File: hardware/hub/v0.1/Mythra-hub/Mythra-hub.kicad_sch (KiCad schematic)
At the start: 2 parts, among them J2 Molex Power Input, U1 TUSB8042A

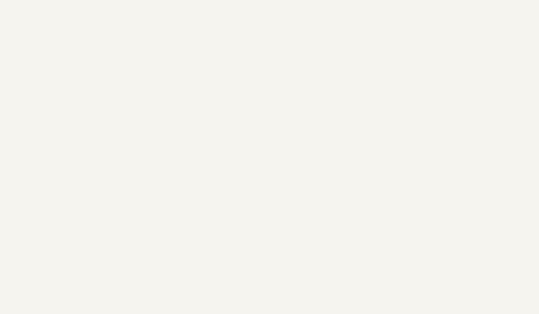
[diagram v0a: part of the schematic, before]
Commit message: Added power delivery control to the DFPs
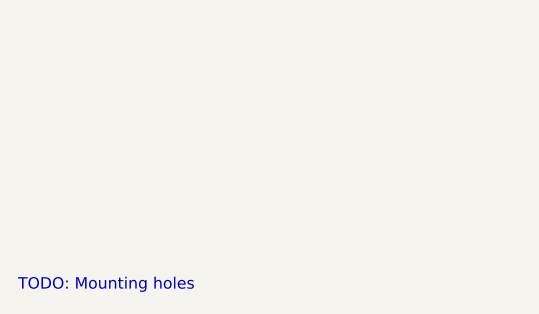
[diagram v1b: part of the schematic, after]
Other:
- note added: "TODO: Mounting holes"

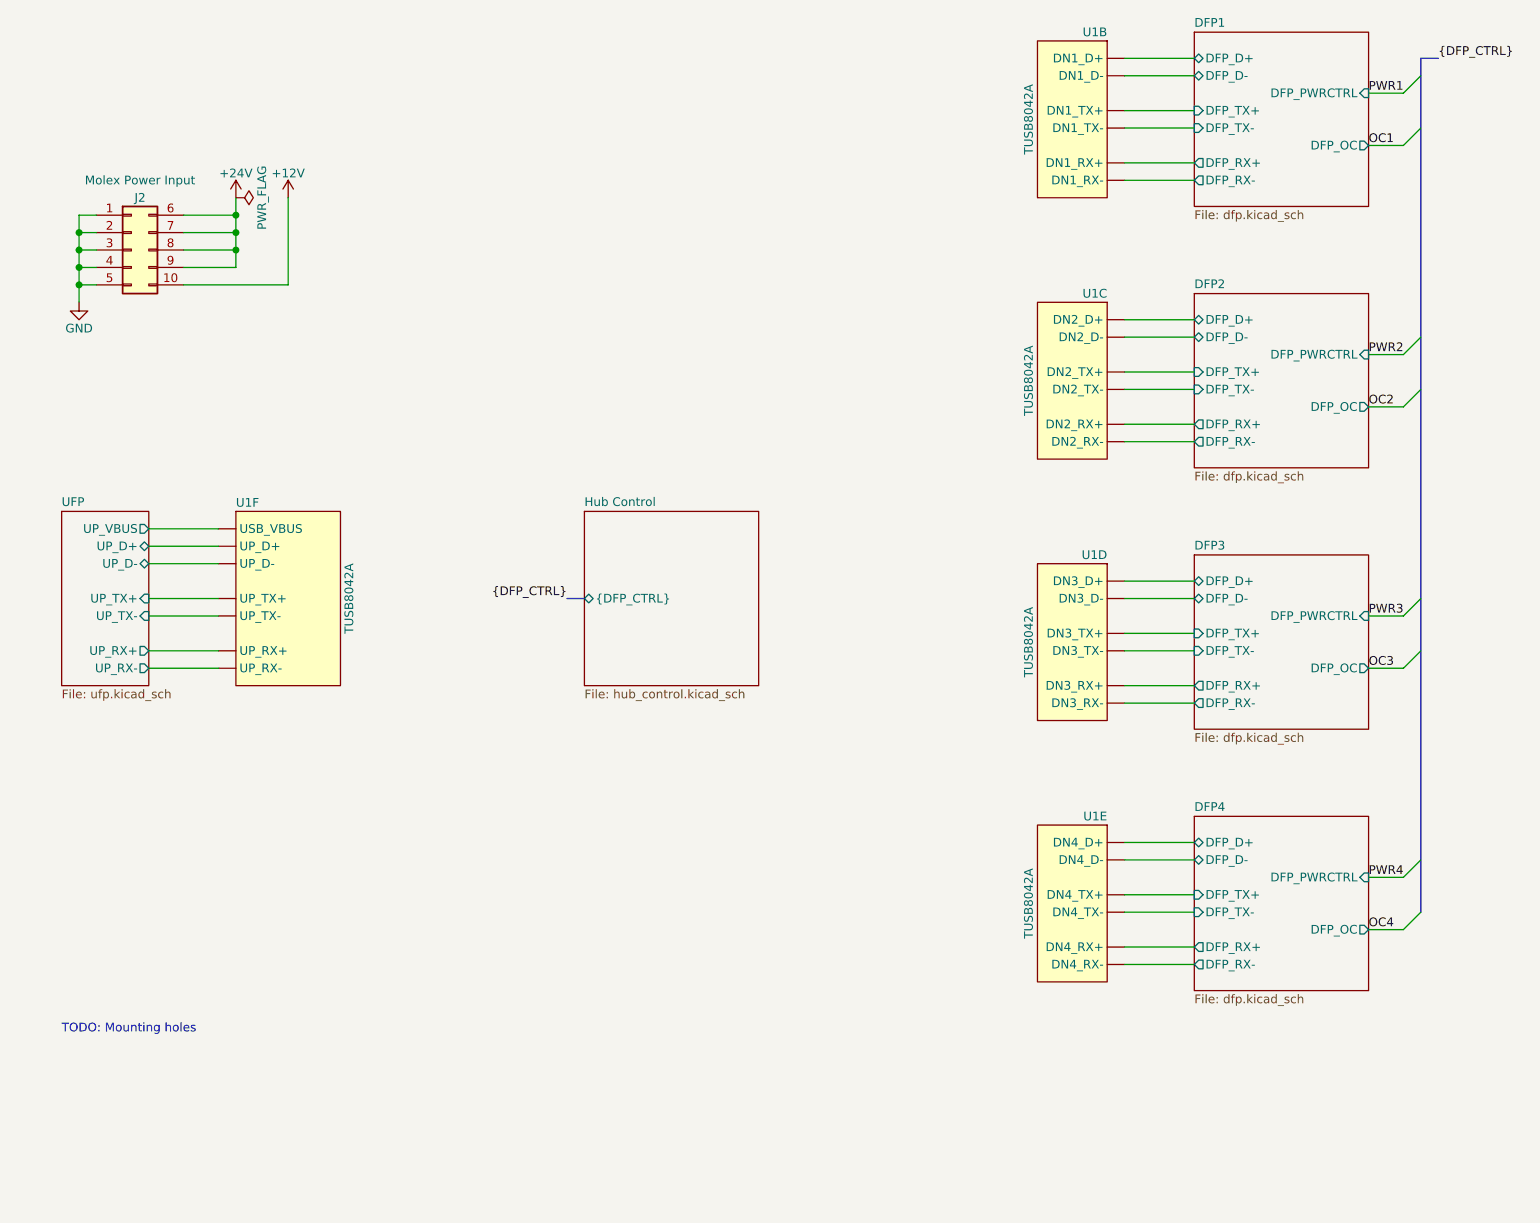
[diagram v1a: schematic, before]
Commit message: Version controlled the changes from the last stream, including the addition of the 3.3V DC-DC, config I2C EEPROM and test points
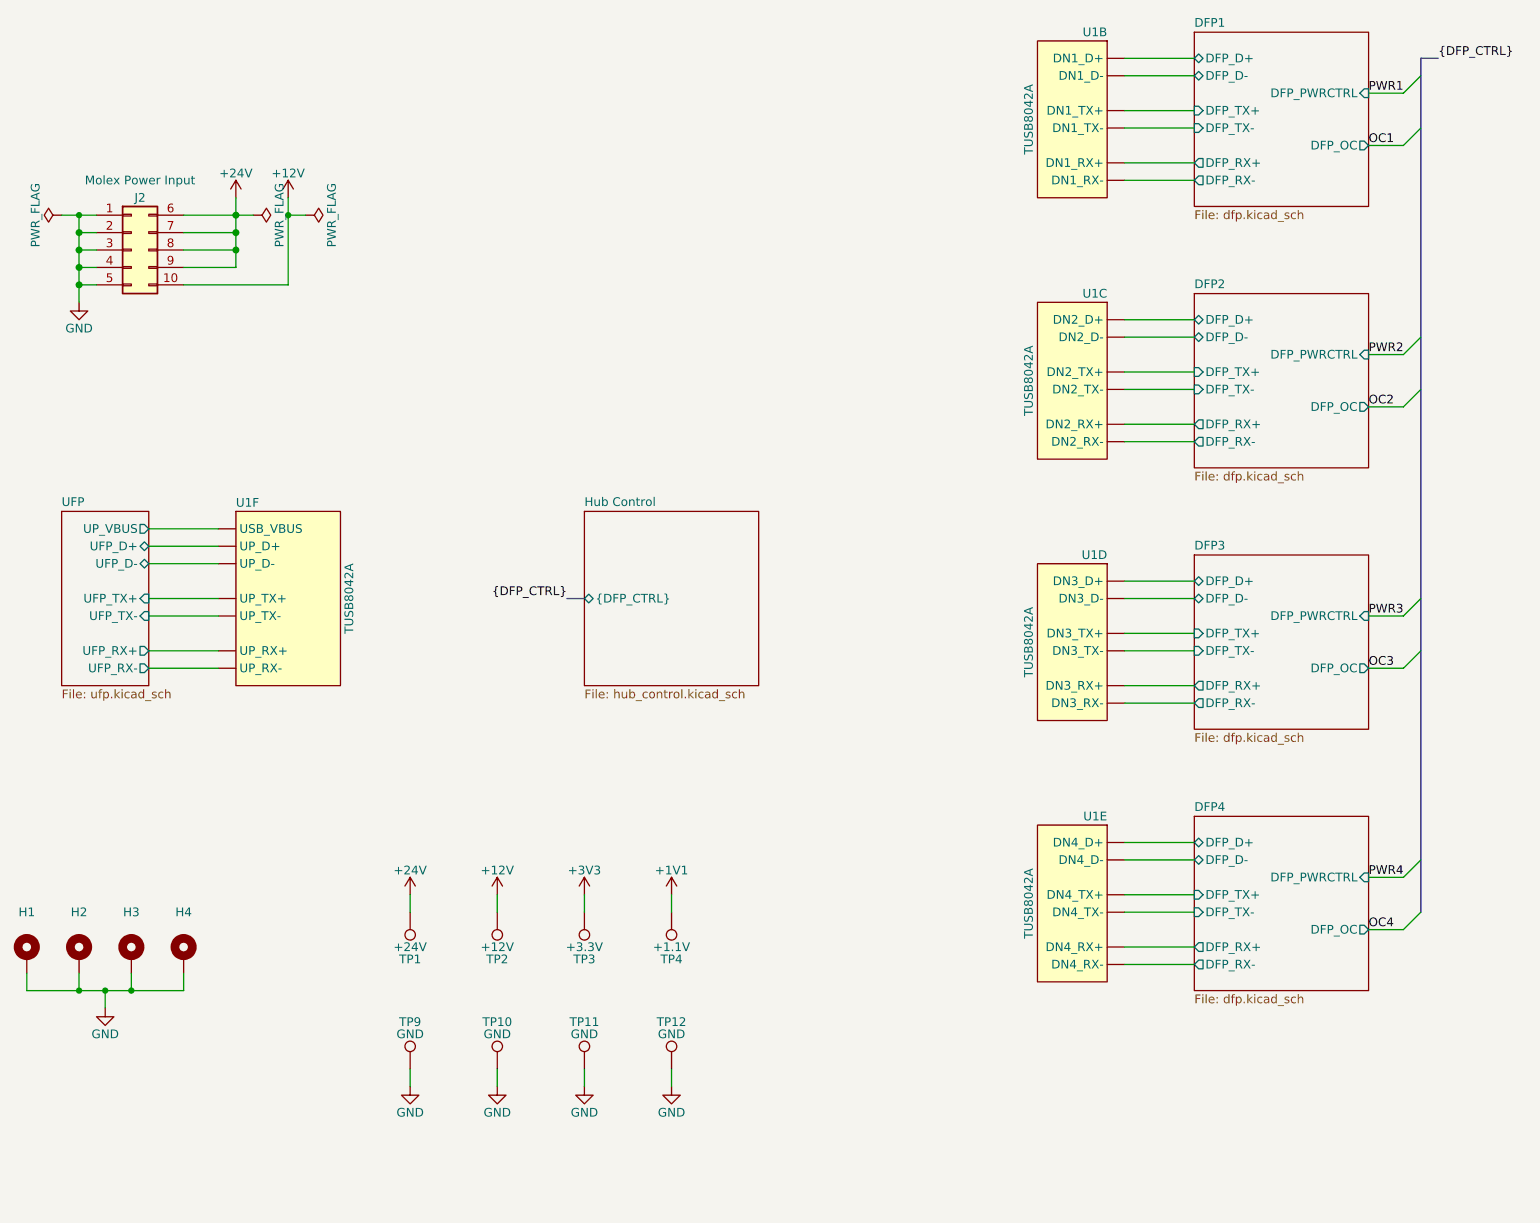
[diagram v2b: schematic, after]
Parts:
- added H1, H2, H3, H4: MountingHole_Pad, MountingHole:MountingHole_3.2mm_M3_Pad, symbol Mechanical:MountingHole_Pad
- added TP1: +24V, TestPoint:TestPoint_Pad_D1.0mm, symbol Connector:TestPoint
- added TP10, TP11, TP12, TP9: GND, TestPoint:TestPoint_Keystone_5019_Minature, symbol Connector:TestPoint
- added TP2: +12V, TestPoint:TestPoint_Pad_D1.0mm, symbol Connector:TestPoint
- added TP3: +3.3V, TestPoint:TestPoint_Pad_D1.0mm, symbol Connector:TestPoint
- added TP4: +1.1V, TestPoint:TestPoint_Pad_D1.0mm, symbol Connector:TestPoint
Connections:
- net +12V: now also TP2.1
- net +24V: now also TP1.1
- net GND: now also H1.1, H2.1, H3.1, H4.1, TP10.1, TP11.1, TP12.1, TP9.1
- net UFP/UP_D+ renamed UFP/UFP_D+
- net UFP/UP_D- renamed UFP/UFP_D-
- net UFP/UP_RX+ renamed UFP/UFP_RX+
- net UFP/UP_RX- renamed UFP/UFP_RX-
- net UFP/UP_TX+ renamed UFP/UFP_TX+
- net UFP/UP_TX- renamed UFP/UFP_TX-
- new net +1V1: TP4.1
- new net +3V3: TP3.1
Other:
- sheet UFP ports: added UFP_D+, UFP_D-, UFP_RX+, UFP_RX-, UFP_TX+, UFP_TX-; removed UP_D+, UP_D-, UP_RX+, UP_RX-, UP_TX+, UP_TX-
- note removed: "TODO: Mounting holes"

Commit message: Finished working through the fab checklists
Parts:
- added TP13, TP14, TP15, TP16: GND, TestPoint:TestPoint_Pad_D1.0mm, symbol Connector:TestPoint
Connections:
- net GND: now also TP13.1, TP14.1, TP15.1, TP16.1
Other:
- moved on the sheet: TP1, TP10, TP11, TP12, TP2, TP3, TP4, TP9

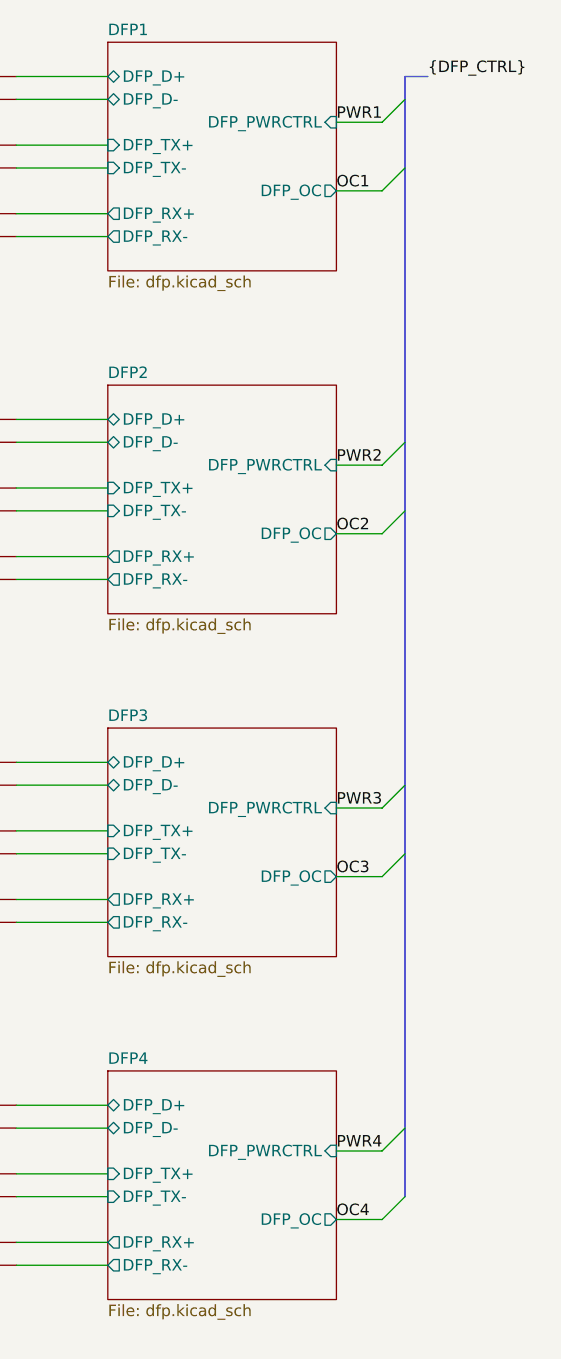
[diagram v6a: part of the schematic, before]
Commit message: Upgraded the schematic files to KiCad 6 format and done some tidy up from the manufacturing crunch
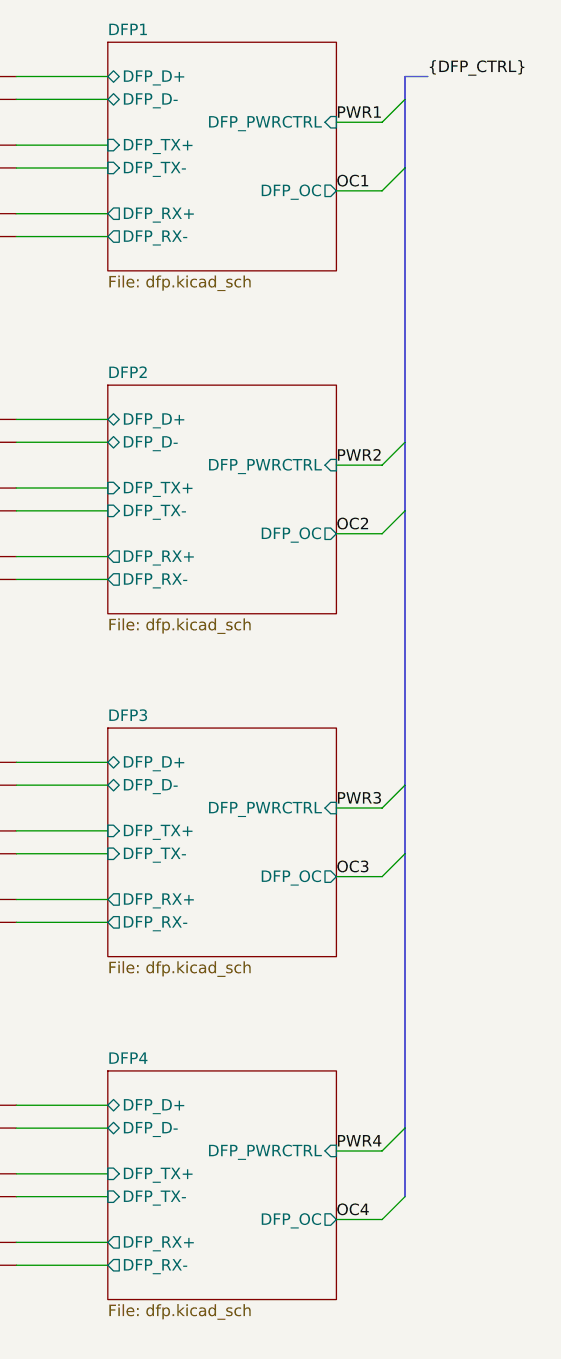
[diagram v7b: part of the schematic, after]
